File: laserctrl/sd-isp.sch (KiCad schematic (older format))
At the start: 26 parts, among them J1 USB, J2 MICROSD, P2 Exhaust, P3 Assist Air, P4 Chiller, P5 ftdi serial, Q1 BC817, Q2 BC817, Q3 BC807, SW1 Program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

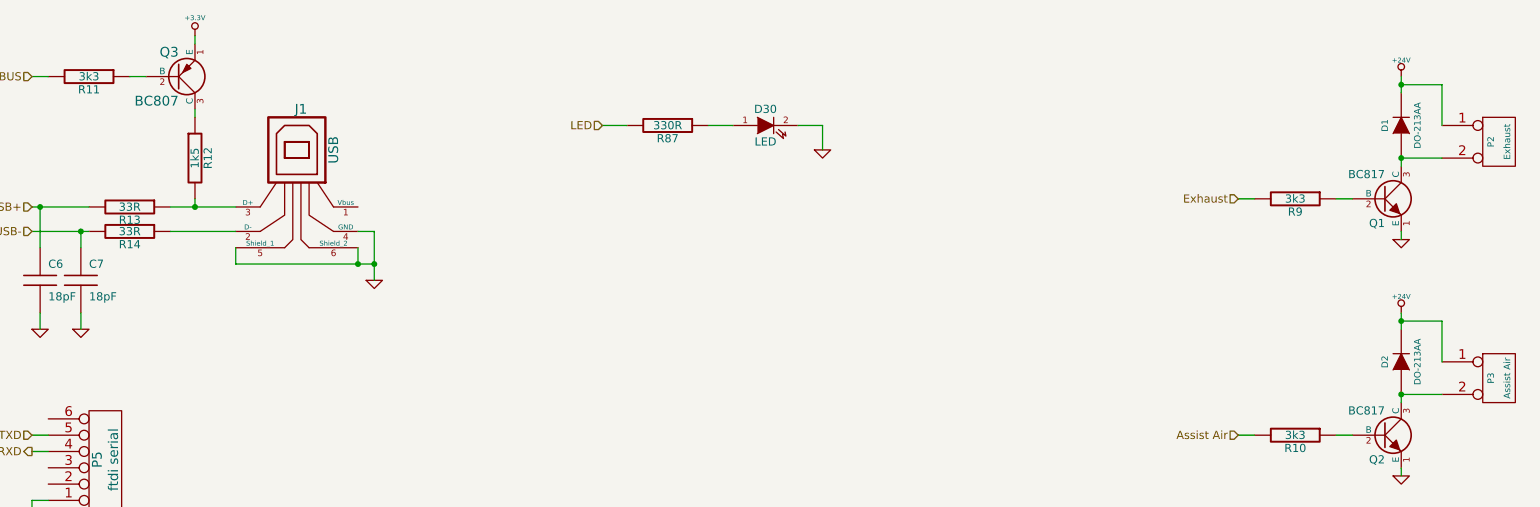
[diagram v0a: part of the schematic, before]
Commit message: Generated the BOM and figured out what parts to buy at ELFA and Mouser
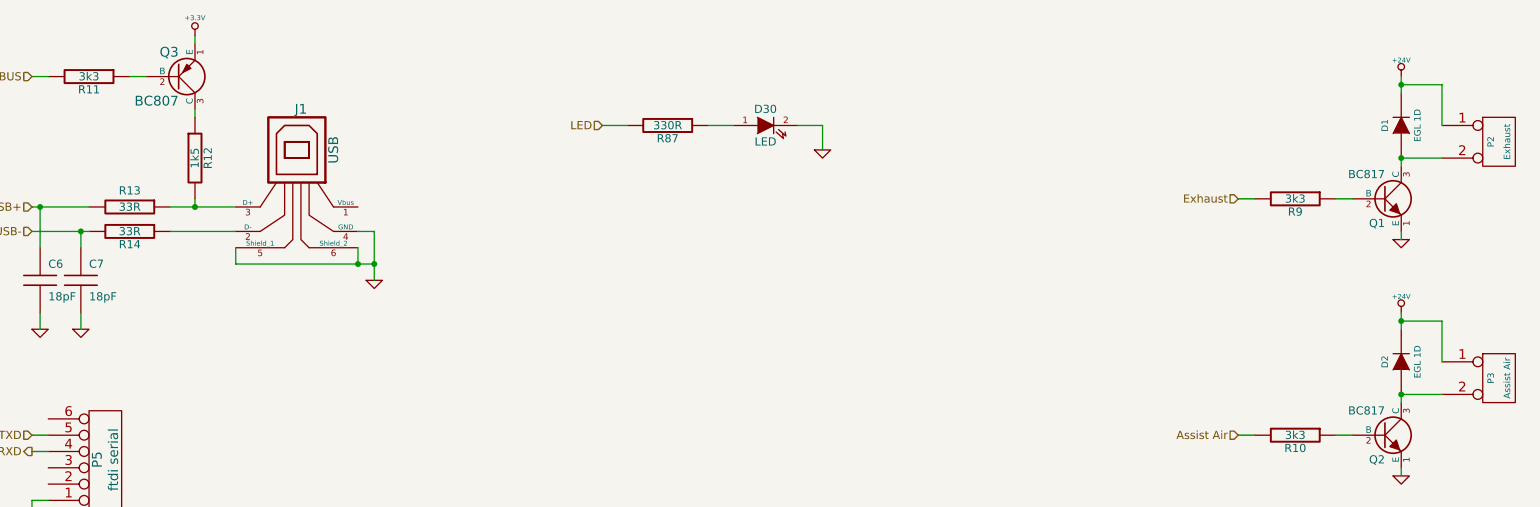
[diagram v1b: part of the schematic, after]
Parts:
- D1, D2: value DO-213AA -> EGL 1D
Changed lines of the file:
@@
-EESchema Schematic File Version 2  date 2011-11-28T22:17:03 CET
+EESchema Schematic File Version 2  date 2011-12-03T21:12:32 CET
 LIBS:power
 LIBS:device
@@
 Sheet 2 10
 Title ""
-Date "27 nov 2011"
+Date "3 dec 2011"
 Rev ""
 Comp ""
@@
 P 9600 2750
 F 0 "D2" H 9600 2850 40  0000 C CNN
-F 1 "DO-213AA" H 9600 2650 40  0000 C CNN
+F 1 "EGL 1D" H 9600 2650 40  0000 C CNN
 	1    9600 2750
 	0    -1   -1   0
@@
 P 9600 1300
 F 0 "D1" H 9600 1400 40  0000 C CNN
-F 1 "DO-213AA" H 9600 1200 40  0000 C CNN
+F 1 "EGL 1D" H 9600 1200 40  0000 C CNN
 	1    9600 1300
 	0    -1   -1   0
@@
 U 1 1 4EB6D1D2
 P 1800 1800
-F 0 "R13" V 1880 1800 50  0000 C CNN
+F 0 "R13" V 1700 1800 50  0000 C CNN
 F 1 "33R" V 1800 1800 50  0000 C CNN
 	1    1800 1800

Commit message: Checked footprints and fixed 1 thinko on the ARM and unfucked the transistor foot prints
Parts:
- removed Q1, Q2: BC817, symbol NPN
- added Q1, Q2: BC817, symbol BC817
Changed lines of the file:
@@
-EESchema Schematic File Version 2  date 2011-12-03T21:12:32 CET
+EESchema Schematic File Version 2  date 2011-12-07T22:22:26 CET
 LIBS:power
 LIBS:device
@@
 LIBS:78l00a
 LIBS:conn_11x2
+LIBS:bc807
+LIBS:bc817
 LIBS:laserctrl-cache
 EELAYER 25  0
@@
 Sheet 2 10
 Title ""
-Date "3 dec 2011"
+Date "7 dec 2011"
 Rev ""
 Comp ""
@@
 Comment4 ""
 $EndDescr
+$Comp
+L BC817 Q2
+U 1 1 4EDFC6CA
+P 9500 3200
+F 0 "Q2" H 9500 3050 50  0000 R CNN
+F 1 "BC817" H 9500 3350 50  0000 R CNN
+	1    9500 3200
+	1    0    0    -1
+$EndComp
+$Comp
+L BC817 Q1
+U 1 1 4EDFC6C7
+P 9500 1750
+F 0 "Q1" H 9500 1600 50  0000 R CNN
+F 1 "BC817" H 9500 1900 50  0000 R CNN
+	1    9500 1750
+	1    0    0    -1
+$EndComp
 NoConn ~ 3150 7400
 NoConn ~ 3000 7400
@@
 $EndComp
 $Comp
-L NPN Q1
-U 1 1 4EBAC039
-P 9500 1750
-F 0 "Q1" H 9500 1600 50  0000 R CNN
-F 1 "BC817" H 9500 1900 50  0000 R CNN
-	1    9500 1750
-	1    0    0    -1
-$EndComp
-$Comp
 L GND #PWR024
 U 1 1 4EBAC038
@@
 	1    0    0    -1
 $EndComp
-$Comp
-L NPN Q2
-U 1 1 4EBAC030
-P 9500 3200
-F 0 "Q2" H 9500 3050 50  0000 R CNN
-F 1 "BC817" H 9500 3350 50  0000 R CNN
-	1    9500 3200
-	1    0    0    -1
-$EndComp

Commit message: Fixed a few bugs in the nxp usbcdc example and got it working, also fixed a couple of boogs in the laserctrl board for V2
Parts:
- Q3: symbol PNP -> BC807
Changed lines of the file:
@@
-EESchema Schematic File Version 2  date 2011-12-07T22:22:26 CET
+EESchema Schematic File Version 2  date 2012-02-15T21:12:24 CET
 LIBS:power
 LIBS:device
@@
 Sheet 2 10
 Title ""
-Date "7 dec 2011"
+Date "15 feb 2012"
 Rev ""
 Comp ""
@@
 $EndComp
 $Comp
-L PNP Q3
+L BC807 Q3
 U 1 1 4EB6D10D
 P 2100 1000

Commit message: Did some more rev2 schematic changes
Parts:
- removed D1, D2: EGL 1D, symbol DIODE
- removed P2: Exhaust, symbol CONN_2
- removed P3: Assist Air, symbol CONN_2
- removed P4: Chiller, symbol CONN_5X2
- removed Q1, Q2: BC817, symbol BC817
- removed Q3: BC807, symbol BC807
- removed R10, R11, R9: 3k3, symbol R
- added K?: Chiller, symbol CONN_3
- added P?: Power, symbol CONN_6
- added Q? (x2): nx3008nbk, symbol MOSFET_N
- added Q? (x2): MOSFET_P, symbol MOSFET_P
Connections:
- net labels added: SDRESET
- wire segments 80 -> 75
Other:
- note removed: "Note: wire 4 sits on the 3.3V logic ground,\n5,6,7 sits on unregulated 24V ground."

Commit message: Completed the schematic changes for rev2 of laserctrl
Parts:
- Q?: value MOSFET_P -> nx3008pbk
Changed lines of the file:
@@
-EESchema Schematic File Version 2  date Sun 14 Oct 2012 04:23:31 PM CEST
+EESchema Schematic File Version 2  date Sun 14 Oct 2012 09:24:14 PM CEST
 LIBS:power
 LIBS:device
@@
 $Descr A4 11700 8267
 encoding utf-8
-Sheet 2 10
+Sheet 3 11
 Title ""
 Date "14 oct 2012"
@@
 P 2100 1000
 F 0 "Q?" H 2100 1190 60  0000 R CNN
-F 1 "MOSFET_P" H 2100 820 60  0000 R CNN
+F 1 "nx3008pbk" H 2100 820 60  0000 R CNN
 	1    2100 1000
 	1    0    0    -1

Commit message: Started redoing the PCB
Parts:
- Q6: renamed from Q?; value MOSFET_P -> nx3008pbk
- gave numbers to parts that had none: 5
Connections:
- wire segments 75 -> 64
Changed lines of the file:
@@
-EESchema Schematic File Version 2  date Sun 14 Oct 2012 09:24:14 PM CEST
+EESchema Schematic File Version 2  date Mon 15 Oct 2012 07:59:43 PM CEST
 LIBS:power
 LIBS:device
@@
 LIBS:vo-2630
 LIBS:little-logic
+LIBS:con-molex
+LIBS:con-molex-2
 LIBS:laserctrl-cache
 EELAYER 25  0
@@
 Sheet 3 11
 Title ""
-Date "14 oct 2012"
+Date "15 oct 2012"
 Rev ""
 Comp ""
@@
 	8850 1800 9600 1800
 Wire Wire Line
-	9400 1400 9500 1400
-Wire Wire Line
-	9500 1400 9600 1400
-Wire Wire Line
-	9400 1700 9500 1700
-Wire Wire Line
-	9500 1700 9600 1700
+	9400 1400 9600 1400
+Wire Wire Line
+	9400 1700 9600 1700
 Wire Wire Line
 	2700 7450 2850 7450
@@
 Connection ~ 2400 4750
 Wire Wire Line
-	2400 4900 2400 4750
-Wire Wire Line
-	2400 4750 2400 4700
+	2400 4900 2400 4700
 Wire Wire Line
 	2400 5300 2400 5400
@@
 	1650 4150 1650 4200
 Wire Wire Line
-	1650 4700 1650 4750
-Wire Wire Line
-	1650 4750 1650 4800
+	1650 4700 1650 4800
 Wire Wire Line
 	1300 3300 1200 3300
@@
 	1500 2050 1500 1950
 Wire Wire Line
-	1550 1950 1500 1950
-Wire Wire Line
-	1500 1950 1200 1950
+	1550 1950 1200 1950
 Connection ~ 3200 2150
 Wire Wire Line
-	3300 2150 3200 2150
-Wire Wire Line
-	3200 2150 2450 2150
+	3300 2150 2450 2150
 Wire Wire Line
 	3200 1950 3300 1950
@@
 	2200 1200 2200 1250
 Wire Wire Line
-	2050 1800 2200 1800
-Wire Wire Line
-	2200 1800 2450 1800
+	2050 1800 2450 1800
 Connection ~ 2200 1800
 Wire Wire Line
@@
 	3200 2050 3200 2150
 Wire Wire Line
-	3300 1950 3300 2150
-Wire Wire Line
-	3300 2150 3300 2250
+	3300 1950 3300 2250
 Connection ~ 3300 2150
 Wire Wire Line
-	1200 1800 1250 1800
-Wire Wire Line
-	1250 1800 1550 1800
+	1200 1800 1550 1800
 Wire Wire Line
 	1250 2050 1250 1800
@@
 	6050 1300 6050 1450
 Wire Wire Line
-	2950 4750 2800 4750
-Wire Wire Line
-	2800 4750 2400 4750
+	2950 4750 2400 4750
 Connection ~ 2800 4750
 Wire Wire Line
 	2400 4150 2400 4200
 Wire Wire Line
-	2700 7500 2700 7450
-Wire Wire Line
-	2700 7450 2700 7400
+	2700 7500 2700 7400
 Connection ~ 2700 7450
 Wire Wire Line
@@
 SDRESET
 $Comp
-L MOSFET_P Q?
+L MOSFET_P Q6
 U 1 1 507AC282
 P 1250 6200
-F 0 "Q?" H 1250 6390 60  0000 R CNN
-F 1 "MOSFET_P" H 1250 6020 60  0000 R CNN
+F 0 "Q6" H 1250 6390 60  0000 R CNN
+F 1 "nx3008pbk" H 1250 6020 60  0000 R CNN
 	1    1250 6200
 	1    0    0    -1
 $EndComp
 $Comp
-L MOSFET_P Q?
+L MOSFET_P Q1
 U 1 1 507AC25D
 P 2100 1000
-F 0 "Q?" H 2100 1190 60  0000 R CNN
+F 0 "Q1" H 2100 1190 60  0000 R CNN
 F 1 "nx3008pbk" H 2100 820 60  0000 R CNN
 	1    2100 1000
@@
 $EndComp
 $Comp
-L GND #PWR?
+L GND #PWR023
 U 1 1 5079779F
 P 9450 3700
-F 0 "#PWR?" H 9450 3700 30  0001 C CNN
+F 0 "#PWR023" H 9450 3700 30  0001 C CNN
 F 1 "GND" H 9450 3630 30  0001 C CNN
 	1    9450 3700
@@
 $EndComp
 $Comp
-L CONN_3 K?
+L CONN_3 K1
 U 1 1 50797786
 P 9950 3800
-F 0 "K?" V 9900 3800 50  0000 C CNN
+F 0 "K1" V 9900 3800 50  0000 C CNN
 F 1 "Chiller" V 10000 3800 40  0000 C CNN
 	1    9950 3800
@@
 $EndComp
 $Comp
-L GND #PWR?
+L GND #PWR024
 U 1 1 5079770C
 P 8850 2950
-F 0 "#PWR?" H 8850 2950 30  0001 C CNN
+F 0 "#PWR024" H 8850 2950 30  0001 C CNN
 F 1 "GND" H 8850 2880 30  0001 C CNN
 	1    8850 2950
@@
 $EndComp
 $Comp
-L MOSFET_N Q?
+L MOSFET_N Q3
 U 1 1 50797702
 P 8750 2650
-F 0 "Q?" H 8700 2850 60  0000 R CNN
+F 0 "Q3" H 8700 2850 60  0000 R CNN
 F 1 "nx3008nbk" H 8650 2450 60  0000 R CNN
 	1    8750 2650
@@
 $EndComp
 $Comp
-L GND #PWR?
+L GND #PWR025
 U 1 1 507976FB
 P 8850 2300
-F 0 "#PWR?" H 8850 2300 30  0001 C CNN
+F 0 "#PWR025" H 8850 2300 30  0001 C CNN
 F 1 "GND" H 8850 2230 30  0001 C CNN
 	1    8850 2300
@@
 $EndComp
 $Comp
-L MOSFET_N Q?
+L MOSFET_N Q2
 U 1 1 507976EB
 P 8750 2000
-F 0 "Q?" H 8700 2200 60  0000 R CNN
+F 0 "Q2" H 8700 2200 60  0000 R CNN
 F 1 "nx3008nbk" H 8650 1800 60  0000 R CNN
 	1    8750 2000
@@
 $EndComp
 $Comp
-L +24V #PWR?
+L +24V #PWR026
 U 1 1 507976CA
 P 9400 1700
-F 0 "#PWR?" H 9400 1650 20  0001 C CNN
+F 0 "#PWR026" H 9400 1650 20  0001 C CNN
 F 1 "+24V" H 9400 1800 30  0000 C CNN
 	1    9400 1700
@@
 $EndComp
 $Comp
-L GND #PWR?
+L GND #PWR027
 U 1 1 507976C5
 P 9400 1400
-F 0 "#PWR?" H 9400 1400 30  0001 C CNN
+F 0 "#PWR027" H 9400 1400 30  0001 C CNN
 F 1 "GND" H 9400 1330 30  0001 C CNN
 	1    9400 1400
@@
 $EndComp
 $Comp
-L CONN_6 P?
+L CONN_6 P3
 U 1 1 507976B9
 P 9950 1650
-F 0 "P?" V 9900 1650 60  0000 C CNN
+F 0 "P3" V 9900 1650 60  0000 C CNN
 F 1 "Power" V 10000 1650 60  0000 C CNN
 	1    9950 1650
@@
 NoConn ~ 3000 7400
 $Comp
-L GND #PWR016
+L GND #PWR028
 U 1 1 4ECEBCDA
 P 2700 7500
-F 0 "#PWR016" H 2700 7500 30  0001 C CNN
+F 0 "#PWR028" H 2700 7500 30  0001 C CNN
 F 1 "GND" H 2700 7430 30  0001 C CNN
 	1    2700 7500
@@
 $EndComp
 $Comp
-L +3.3V #PWR017
+L +3.3V #PWR029
 U 1 1 4EC159D5
 P 2400 4150
-F 0 "#PWR017" H 2400 4110 30  0001 C CNN
+F 0 "#PWR029" H 2400 4110 30  0001 C CNN
 F 1 "+3.3V" H 2400 4260 30  0000 C CNN
 	1    2400 4150
@@
 $EndComp
 $Comp
-L GND #PWR018
+L GND #PWR030
 U 1 1 4EBEC7BB
 P 6050 1450
-F 0 "#PWR018" H 6050 1450 30  0001 C CNN
+F 0 "#PWR030" H 6050 1450 30  0001 C CNN
 F 1 "GND" H 6050 1380 30  0001 C CNN
 	1    6050 1450
@@
 $EndComp
 $Comp
-L GND #PWR027
+L GND #PWR031
 U 1 1 4EB6DA7E
 P 1850 6700
-F 0 "#PWR027" H 1850 6700 30  0001 C CNN
+F 0 "#PWR031" H 1850 6700 30  0001 C CNN
 F 1 "GND" H 1850 6630 30  0001 C CNN
 	1    1850 6700
@@
 $EndComp
 $Comp
-L +3.3V #PWR028
+L +3.3V #PWR032
 U 1 1 4EB6DA5E
 P 1350 5950
-F 0 "#PWR028" H 1350 5910 30  0001 C CNN
+F 0 "#PWR032" H 1350 5910 30  0001 C CNN
 F 1 "+3.3V" H 1350 6060 30  0000 C CNN
 	1    1350 5950
@@
 CS
 $Comp
-L GND #PWR029
+L GND #PWR033
 U 1 1 4EB6D76C
 P 2800 5500
-F 0 "#PWR029" H 2800 5500 30  0001 C CNN
+F 0 "#PWR033" H 2800 5500 30  0001 C CNN
 F 1 "GND" H 2800 5430 30  0001 C CNN
 	1    2800 5500
@@
 $EndComp
 $Comp
-L +3.3V #PWR030
+L +3.3V #PWR034
 U 1 1 4EB6D47F
 P 1650 4150
-F 0 "#PWR030" H 1650 4110 30  0001 C CNN
+F 0 "#PWR034" H 1650 4110 30  0001 C CNN
 F 1 "+3.3V" H 1650 4260 30  0000 C CNN
 	1    1650 4150
@@
 $EndComp
 $Comp
-L GND #PWR031
+L GND #PWR035
 U 1 1 4EB6D436
 P 1650 5500
-F 0 "#PWR031" H 1650 5500 30  0001 C CNN
+F 0 "#PWR035" H 1650 5500 30  0001 C CNN
 F 1 "GND" H 1650 5430 30  0001 C CNN
 	1    1650 5500
@@
 $EndComp
 $Comp
-L GND #PWR032
+L GND #PWR036
 U 1 1 4EB6D3CA
 P 1200 3700
-F 0 "#PWR032" H 1200 3700 30  0001 C CNN
+F 0 "#PWR036" H 1200 3700 30  0001 C CNN
 F 1 "GND" H 1200 3630 30  0001 C CNN
 	1    1200 3700
@@
 ~RESET
 $Comp
-L GND #PWR033
+L GND #PWR037
 U 1 1 4EB6D202
 P 1500 2550
-F 0 "#PWR033" H 1500 2550 30  0001 C CNN
+F 0 "#PWR037" H 1500 2550 30  0001 C CNN
 F 1 "GND" H 1500 2480 30  0001 C CNN
 	1    1500 2550
@@
 $EndComp
 $Comp
-L GND #PWR034
+L GND #PWR038
 U 1 1 4EB6D1FB
 P 1250 2550
-F 0 "#PWR034" H 1250 2550 30  0001 C CNN
+F 0 "#PWR038" H 1250 2550 30  0001 C CNN
 F 1 "GND" H 1250 2480 30  0001 C CNN
 	1    1250 2550
@@
 $EndComp
 $Comp
-L GND #PWR035
+L GND #PWR039
 U 1 1 4EB6D1B5
 P 3300 2250
-F 0 "#PWR035" H 3300 2250 30  0001 C CNN
+F 0 "#PWR039" H 3300 2250 30  0001 C CNN
 F 1 "GND" H 3300 2180 30  0001 C CNN
 	1    3300 2250
@@
 $EndComp
 $Comp
-L +3.3V #PWR036
+L +3.3V #PWR040
 U 1 1 4EB6D11C
 P 2200 750
-F 0 "#PWR036" H 2200 710 30  0001 C CNN
+F 0 "#PWR040" H 2200 710 30  0001 C CNN
 F 1 "+3.3V" H 2200 860 30  0000 C CNN
 	1    2200 750
